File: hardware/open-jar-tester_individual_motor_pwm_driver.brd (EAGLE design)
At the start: 20.3 x 20.3 mm, 6 parts

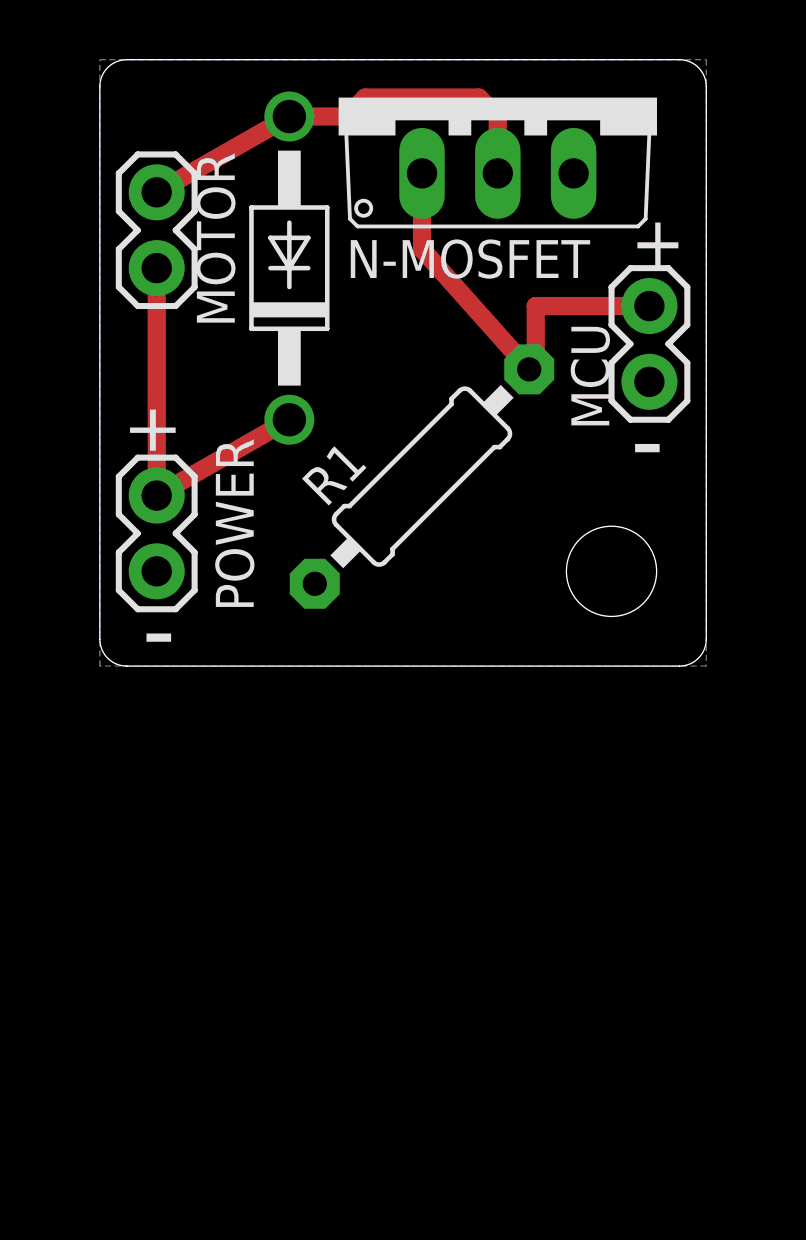
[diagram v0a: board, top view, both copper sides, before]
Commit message: shuffling files into folders
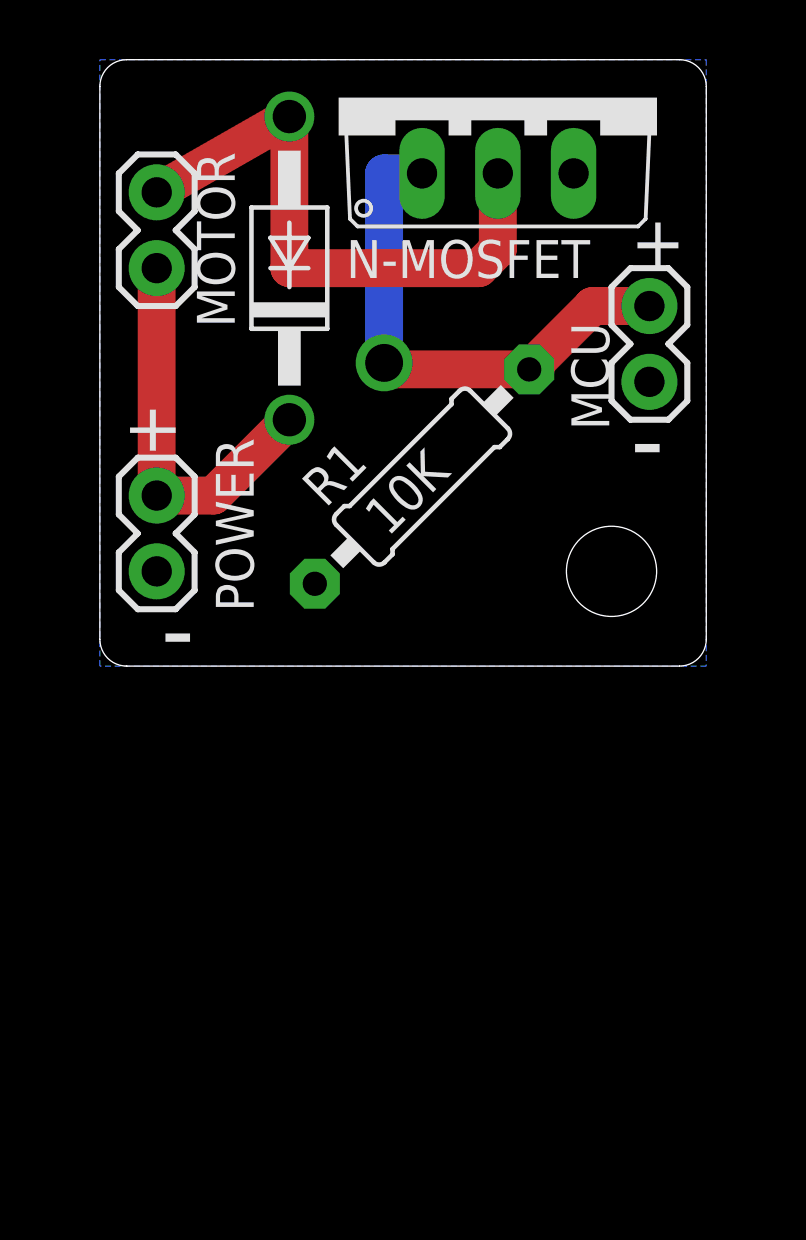
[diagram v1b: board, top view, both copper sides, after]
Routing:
- net N$3: track 14.5 -> 20.0 mm
- net N$2: track 14.1 -> 17.6 mm, vias 0 -> 1
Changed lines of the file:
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@@
 <hole x="17.145" y="3.175" drill="3.0226"/>
 <text x="2.54" y="6.985" size="1.778" layer="21" rot="R90">+</text>
-<text x="2.54" y="2.54" size="2.54" layer="21" rot="R180">-</text>
+<text x="3.175" y="2.54" size="2.54" layer="21" rot="R180">-</text>
 <text x="17.78" y="6.35" size="2.54" layer="21">-</text>
 <text x="17.78" y="13.335" size="1.778" layer="21">+</text>
@@
 </element>
 <element name="N-MOSFET" library="adafruit" package="TO220V" value="" x="13.335" y="19.05"/>
-<element name="R1" library="adafruit" package="0207/10" value="10K" x="10.795" y="6.35" rot="R45"/>
+<element name="R1" library="adafruit" package="0207/10" value="10K" x="10.795" y="6.35" smashed="yes" rot="R45">
+<attribute name="NAME" x="7.56210625" y="5.27236875" size="1.27" layer="25" ratio="10" rot="R45"/>
+<attribute name="VALUE" x="9.645525" y="4.3025" size="1.27" layer="25" ratio="10" rot="R45"/>
+</element>
 </elements>
 <signals>
@@
 <contactref element="MCU" pad="1"/>
 <contactref element="R1" pad="2"/>
-<wire x1="10.795" y1="16.51" x2="10.795" y2="13.97" width="0.6096" layer="1"/>
-<wire x1="10.795" y1="13.97" x2="14.3871" y2="9.9421" width="0.6096" layer="1"/>
 <wire x1="14.3871" y1="9.9421" x2="14.605" y2="9.9421" width="0.6096" layer="1"/>
-<wire x1="14.605" y1="9.9421" x2="14.605" y2="12.065" width="0.6096" layer="1"/>
-<wire x1="14.605" y1="12.065" x2="18.415" y2="12.065" width="0.6096" layer="1"/>
+<wire x1="14.605" y1="9.9421" x2="14.605" y2="10.16" width="1.27" layer="1"/>
+<wire x1="14.605" y1="10.16" x2="16.51" y2="12.065" width="1.27" layer="1"/>
+<wire x1="16.51" y1="12.065" x2="18.415" y2="12.065" width="1.27" layer="1"/>
+<wire x1="14.3871" y1="9.9421" x2="9.7429" y2="9.9421" width="1.27" layer="1"/>
+<wire x1="9.7429" y1="9.9421" x2="9.525" y2="10.16" width="1.27" layer="1"/>
+<wire x1="9.525" y1="10.16" x2="9.525" y2="16.51" width="1.27" layer="16"/>
+<wire x1="9.525" y1="16.51" x2="10.795" y2="16.51" width="1.27" layer="16"/>
+<via x="9.525" y="10.16" extent="1-16" drill="1.27"/>
 </signal>
 <signal name="N$4">
@@
 <contactref element="POWER" pad="2"/>
 <contactref element="D1" pad="C"/>
-<wire x1="1.905" y1="13.335" x2="1.905" y2="5.715" width="0.6096" layer="1"/>
-<wire x1="6.35" y1="8.255" x2="1.905" y2="5.715" width="0.6096" layer="1"/>
+<wire x1="1.905" y1="13.335" x2="1.905" y2="5.715" width="1.27" layer="1"/>
+<wire x1="1.905" y1="5.715" x2="3.81" y2="5.715" width="1.27" layer="1"/>
+<wire x1="3.81" y1="5.715" x2="6.35" y2="8.255" width="1.27" layer="1"/>
 </signal>
 <signal name="N$3">
@@
 <contactref element="D1" pad="A"/>
 <contactref element="N-MOSFET" pad="2"/>
-<wire x1="1.905" y1="15.875" x2="6.35" y2="18.415" width="0.6096" layer="1"/>
-<wire x1="6.35" y1="18.415" x2="8.255" y2="18.415" width="0.6096" layer="1"/>
-<wire x1="8.255" y1="18.415" x2="8.89" y2="19.05" width="0.6096" layer="1"/>
-<wire x1="8.89" y1="19.05" x2="12.7" y2="19.05" width="0.6096" layer="1"/>
-<wire x1="12.7" y1="19.05" x2="13.335" y2="18.415" width="0.6096" layer="1"/>
-<wire x1="13.335" y1="18.415" x2="13.335" y2="16.51" width="0.6096" layer="1"/>
+<wire x1="1.905" y1="15.875" x2="6.35" y2="18.415" width="1.27" layer="1"/>
+<wire x1="6.35" y1="18.415" x2="6.35" y2="13.335" width="1.27" layer="1"/>
+<wire x1="6.35" y1="13.335" x2="12.7" y2="13.335" width="1.27" layer="1"/>
+<wire x1="12.7" y1="13.335" x2="13.335" y2="13.97" width="1.27" layer="1"/>
+<wire x1="13.335" y1="13.97" x2="13.335" y2="16.51" width="1.27" layer="1"/>
 </signal>
 <signal name="GND">

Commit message: deleting temp files
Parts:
- added BEMF_ADC: (no value), SparkFun-Connectors:1X01
- added C1, C2: (no value), SparkFun-Passives:CAP-PTH-SMALL
- added R2: 10K, adafruit:0207/10
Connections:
- new net N$1: BEMF_ADC.1, C2.2, R2.1
- net GND: now also C1.2, C2.1
- net N$3: now also R2.2
- net N$4: now also C1.1
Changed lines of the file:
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@@
 <attribute name="VALUE" x="9.645525" y="4.3025" size="1.27" layer="25" ratio="10" rot="R45"/>
 </element>
+<element name="C1" library="SparkFun-Passives" package="CAP-PTH-SMALL" value="" x="1.27" y="-3.175"/>
+<element name="R2" library="adafruit" package="0207/10" value="10K" x="6.35" y="-7.62"/>
+<element name="C2" library="SparkFun-Passives" package="CAP-PTH-SMALL" value="" x="1.27" y="-10.795"/>
+<element name="BEMF_ADC" library="SparkFun-Connectors" package="1X01" value="" x="1.905" y="-15.875"/>
 </elements>
 <signals>
@@
 <wire x1="1.905" y1="5.715" x2="3.81" y2="5.715" width="1.27" layer="1"/>
 <wire x1="3.81" y1="5.715" x2="6.35" y2="8.255" width="1.27" layer="1"/>
+<contactref element="C1" pad="1"/>
+<wire x1="1.27" y1="-3.175" x2="1.905" y2="5.715" width="0" layer="19" extent="1-1"/>
 </signal>
 <signal name="N$3">
@@
 <wire x1="12.7" y1="13.335" x2="13.335" y2="13.97" width="1.27" layer="1"/>
 <wire x1="13.335" y1="13.97" x2="13.335" y2="16.51" width="1.27" layer="1"/>
+<contactref element="R2" pad="2"/>
+<wire x1="11.43" y1="-7.62" x2="12.7" y2="13.335" width="0" layer="19" extent="1-1"/>
 </signal>
 <signal name="GND">
@@
 <contactref element="N-MOSFET" pad="3"/>
 <contactref element="R1" pad="1"/>
+<contactref element="C1" pad="2"/>
+<contactref element="C2" pad="1"/>
+<wire x1="18.415" y1="9.525" x2="15.875" y2="16.51" width="0" layer="19" extent="1-1"/>
+<wire x1="7.202896875" y1="2.757896875" x2="18.415" y2="9.525" width="0" layer="19" extent="1-1"/>
+<wire x1="1.905" y1="3.175" x2="7.202896875" y2="2.757896875" width="0" layer="19" extent="1-1"/>
+<wire x1="3.81" y1="-3.175" x2="1.905" y2="3.175" width="0" layer="19" extent="1-1"/>
+<wire x1="1.27" y1="-10.795" x2="3.81" y2="-3.175" width="0" layer="19" extent="1-1"/>
+</signal>
+<signal name="N$1">
+<contactref element="R2" pad="1"/>
+<contactref element="C2" pad="2"/>
+<contactref element="BEMF_ADC" pad="1"/>
+<wire x1="3.81" y1="-10.795" x2="1.905" y2="-15.875" width="0" layer="19" extent="1-1"/>
+<wire x1="1.27" y1="-7.62" x2="3.81" y2="-10.795" width="0" layer="19" extent="1-1"/>
 </signal>
 </signals>
